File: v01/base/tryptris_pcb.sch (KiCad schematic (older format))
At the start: 131 parts, among them J1 USB_C_Receptacle_USB2.0, J2 I2C-L, J3 I2C-R, SW1 Reset, U1 ATmega32U4-AU, U2 MCP23017_SO, Y1 16Mhz

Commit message: Update base model to use parts from lcsc
The footprints for USB ports had to change as I can't get the previous
footprint shape from lcsc.
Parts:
- J1, J2, J3: footprint Type-C:USB_C_GCT_USB4085 -> Connector_USB:USB_C_Receptacle_HRO_TYPE-C-31-M-12
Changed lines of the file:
@@
 F 0 "J1" H 5207 2517 50  0000 C CNN
 F 1 "USB_C_Receptacle_USB2.0" H 5207 2426 50  0000 C CNN
-F 2 "Type-C:USB_C_GCT_USB4085" H 5250 1650 50  0001 C CNN
+F 2 "Connector_USB:USB_C_Receptacle_HRO_TYPE-C-31-M-12" H 5250 1650 50  0001 C CNN
 F 3 "https://www.usb.org/sites/default/files/documents/usb_type-c.zip" H 5250 1650 50  0001 C CNN
 	1    5100 1650
@@
 F 0 "J2" H 5357 5917 50  0000 C CNN
 F 1 "I2C-L" H 5357 5826 50  0000 C CNN
-F 2 "Type-C:USB_C_GCT_USB4085" H 5400 5050 50  0001 C CNN
+F 2 "Connector_USB:USB_C_Receptacle_HRO_TYPE-C-31-M-12" H 5400 5050 50  0001 C CNN
 F 3 "https://www.usb.org/sites/default/files/documents/usb_type-c.zip" H 5400 5050 50  0001 C CNN
 	1    5250 5050
@@
 F 0 "J3" H 4907 8217 50  0000 C CNN
 F 1 "I2C-R" H 4907 8126 50  0000 C CNN
-F 2 "Type-C:USB_C_GCT_USB4085" H 4950 7350 50  0001 C CNN
+F 2 "Connector_USB:USB_C_Receptacle_HRO_TYPE-C-31-M-12" H 4950 7350 50  0001 C CNN
 F 3 "https://www.usb.org/sites/default/files/documents/usb_type-c.zip" H 4950 7350 50  0001 C CNN
 	1    4800 7350

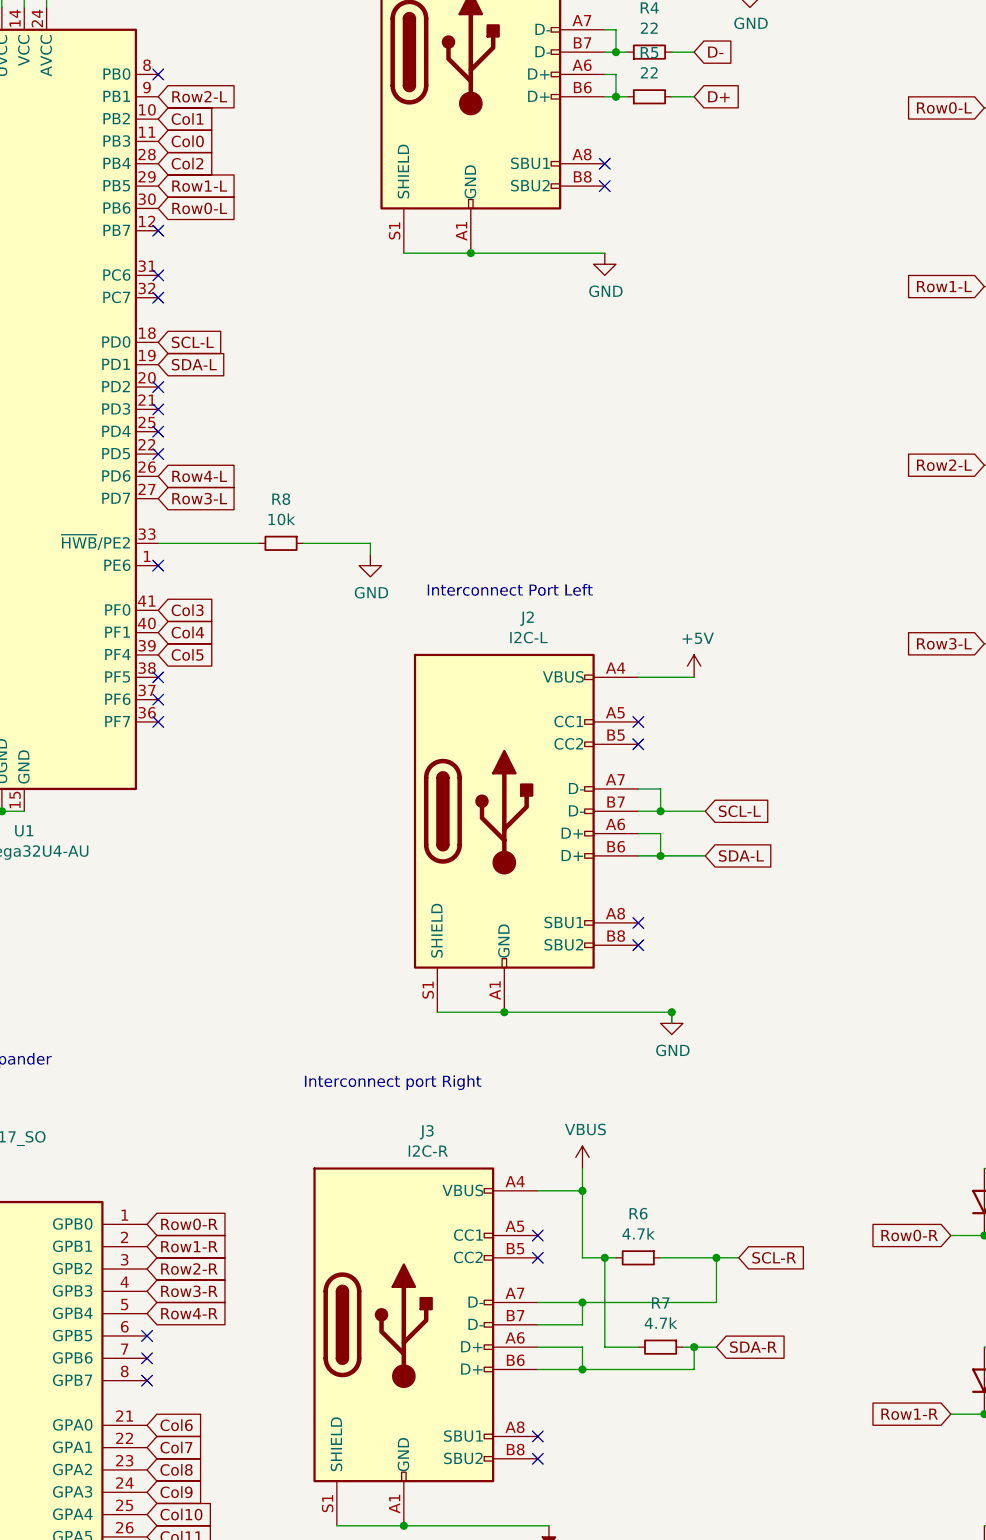
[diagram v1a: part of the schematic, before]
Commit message: Move I2C resistors to MCU side
This lets the right side be simpler and visually cleaner. It also
matches the component layout of the bling version.
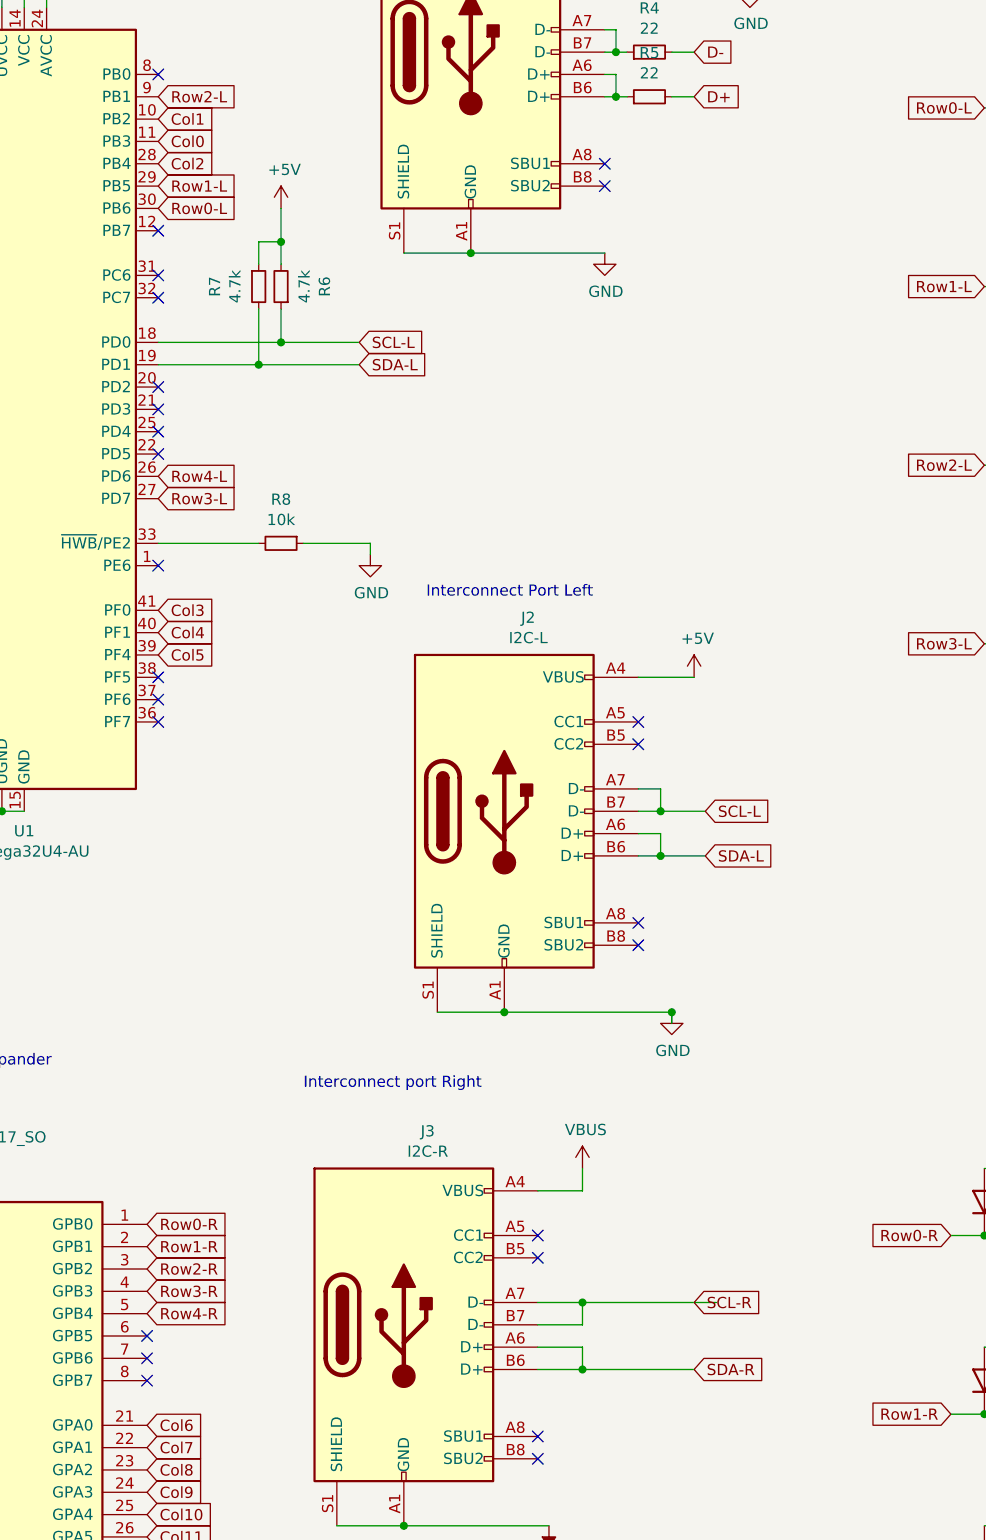
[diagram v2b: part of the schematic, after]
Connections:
- net +5V: now also R6.2, R7.1
- net SCL-L: now also R6.1
- net SCL-R: no longer R6.1
- net SDA-L: now also R7.2
- net SDA-R: no longer R7.1
- net VBUS: no longer R6.2, R7.2
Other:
- moved on the sheet: R6, R7
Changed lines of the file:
@@
 Text GLabel 2250 7000 0    50   Input ~ 0
 SCL-R
-Text GLabel 3700 3050 2    50   Input ~ 0
+Text GLabel 4600 3050 2    50   Input ~ 0
 SDA-L
-Text GLabel 3700 2950 2    50   Input ~ 0
+Text GLabel 4600 2950 2    50   Input ~ 0
 SCL-L
 Text Notes 4350 6300 0    50   ~ 0
@@
 Wire Wire Line
 	5600 6750 5600 6650
-Wire Wire Line
-	5600 7050 5700 7050
-Wire Wire Line
-	6200 7050 6300 7050
-Connection ~ 6200 7050
-Wire Wire Line
-	5950 7050 6200 7050
 $Comp
 L Device:R_Small R6
 U 1 1 615E83A9
-P 5850 7050
-F 0 "R6" V 5654 7050 50  0000 C CNN
-F 1 "4.7k" V 5745 7050 50  0000 C CNN
-F 2 "Resistor_SMD:R_0805_2012Metric" H 5850 7050 50  0001 C CNN
-F 3 "~" H 5850 7050 50  0001 C CNN
-	1    5850 7050
-	0    1    1    0
-$EndComp
-Text GLabel 6300 7050 2    50   Input ~ 0
+P 4250 2700
+F 0 "R6" V 4054 2700 50  0000 C CNN
+F 1 "4.7k" V 4145 2700 50  0000 C CNN
+F 2 "Resistor_SMD:R_0805_2012Metric" H 4250 2700 50  0001 C CNN
+F 3 "~" H 4250 2700 50  0001 C CNN
+	1    4250 2700
+	-1   0    0    1
+$EndComp
+Text GLabel 6100 7250 2    50   Input ~ 0
 SCL-R
 Wire Wire Line
 	5600 7250 6200 7250
-Wire Wire Line
-	6200 7050 6200 7250
 Connection ~ 5600 7250
-Wire Wire Line
-	5600 6750 5600 7050
-Connection ~ 5600 6750
-Wire Wire Line
-	6100 7450 6200 7450
-Connection ~ 6100 7450
-Wire Wire Line
-	6100 7550 6100 7450
-Wire Wire Line
-	6050 7450 6100 7450
 $Comp
 L Device:R_Small R7
 U 1 1 61698CA9
-P 5950 7450
-F 0 "R7" V 5754 7450 50  0000 C CNN
-F 1 "4.7k" V 5845 7450 50  0000 C CNN
-F 2 "Resistor_SMD:R_0805_2012Metric" H 5950 7450 50  0001 C CNN
-F 3 "~" H 5950 7450 50  0001 C CNN
-	1    5950 7450
-	0    1    1    0
-$EndComp
-Text GLabel 6200 7450 2    50   Input ~ 0
+P 4150 2700
+F 0 "R7" V 3954 2700 50  0000 C CNN
+F 1 "4.7k" V 4045 2700 50  0000 C CNN
+F 2 "Resistor_SMD:R_0805_2012Metric" H 4150 2700 50  0001 C CNN
+F 3 "~" H 4150 2700 50  0001 C CNN
+	1    4150 2700
+	1    0    0    -1
+$EndComp
+Text GLabel 6100 7550 2    50   Input ~ 0
 SDA-R
 Wire Wire Line
 	5600 7550 6100 7550
 Connection ~ 5600 7550
-Wire Wire Line
-	5700 7050 5700 7450
-Wire Wire Line
-	5700 7450 5850 7450
-Connection ~ 5700 7050
-Wire Wire Line
-	5700 7050 5750 7050
 NoConn ~ 5850 5550
 NoConn ~ 5850 5650
@@
 NoConn ~ 5400 7850
 NoConn ~ 5400 7950
+Wire Wire Line
+	3700 2950 4250 2950
+Wire Wire Line
+	3700 3050 4150 3050
+Wire Wire Line
+	4150 2800 4150 3050
+Connection ~ 4150 3050
+Wire Wire Line
+	4150 3050 4600 3050
+Wire Wire Line
+	4250 2800 4250 2950
+Connection ~ 4250 2950
+Wire Wire Line
+	4250 2950 4600 2950
+$Comp
+L power:+5V #PWR?
+U 1 1 617063DF
+P 4250 2350
+F 0 "#PWR?" H 4250 2200 50  0001 C CNN
+F 1 "+5V" H 4265 2523 50  0000 C CNN
+F 2 "" H 4250 2350 50  0001 C CNN
+F 3 "" H 4250 2350 50  0001 C CNN
+	1    4250 2350
+	1    0    0    -1
+$EndComp
+Wire Wire Line
+	4250 2350 4250 2500
+Wire Wire Line
+	4250 2500 4150 2500
+Wire Wire Line
+	4150 2500 4150 2600
+Connection ~ 4250 2500
+Wire Wire Line
+	4250 2500 4250 2600
 $EndSCHEMATC

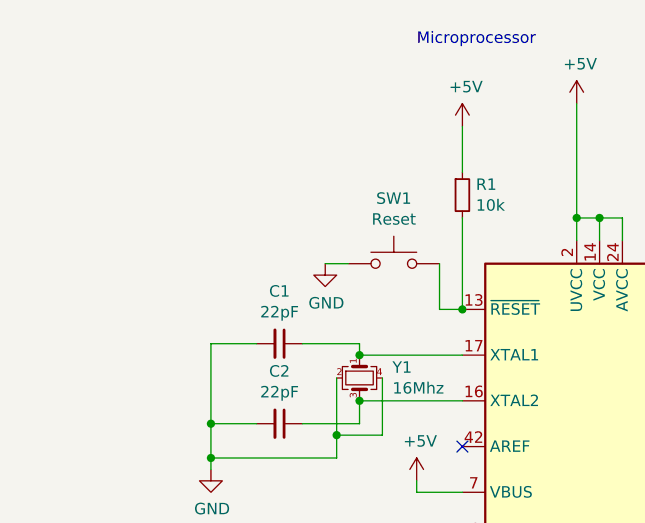
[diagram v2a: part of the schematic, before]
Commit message: Add ISP connector to base board.
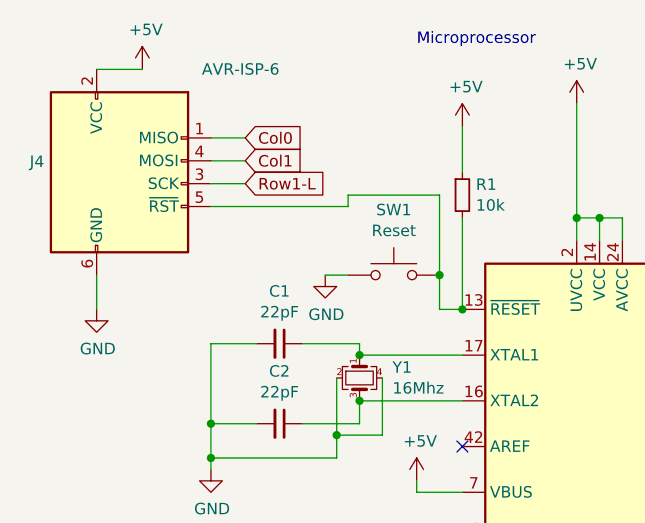
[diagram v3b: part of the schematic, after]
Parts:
- added J4: AVR-ISP-6, random-keyboard-parts:Reset_Pretty-Mask, symbol Connector:AVR-ISP-6
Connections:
- net +5V: now also J4.2 (VCC)
- net Col0: now also J4.1 (MISO)
- net Col1: now also J4.4 (MOSI)
- net GND: now also J4.6 (GND)
- net Row1-L: now also J4.3 (SCK)
- net at R1.2, SW1.2, U1.13 (~RESET): now also J4.5 (~RST)
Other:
- moved on the sheet: SW1
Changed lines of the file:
@@
 $EndDescr
-$Comp
-L MCU_Microchip_ATmega:ATmega32U4-AU U1
-U 1 1 60F2601E
-P 3100 3250
-F 0 "U1" H 3100 1361 50  0000 C CNN
-F 1 "ATmega32U4-AU" H 3100 1270 50  0000 C CNN
-F 2 "Package_QFP:TQFP-44_10x10mm_P0.8mm" H 3100 3250 50  0001 C CIN
-F 3 "http://ww1.microchip.com/downloads/en/DeviceDoc/Atmel-7766-8-bit-AVR-ATmega16U4-32U4_Datasheet.pdf" H 3100 3250 50  0001 C CNN
-	1    3100 3250
-	1    0    0    -1
-$EndComp
 $Comp
 L power:+5V #PWR0101
@@
 L Switch:SW_Push SW1
 U 1 1 60F454A1
-P 2200 1550
-F 0 "SW1" H 2200 1835 50  0000 C CNN
-F 1 "Reset" H 2200 1744 50  0000 C CNN
-F 2 "Keebio-Parts:SW_SPST_TL3342" H 2200 1750 50  0001 C CNN
-F 3 "~" H 2200 1750 50  0001 C CNN
-	1    2200 1550
-	1    0    0    -1
-$EndComp
-Wire Wire Line
-	2400 1550 2400 1750
-Wire Wire Line
-	2400 1750 2500 1750
+P 2200 1600
+F 0 "SW1" H 2200 1885 50  0000 C CNN
+F 1 "Reset" H 2200 1794 50  0000 C CNN
+F 2 "Keebio-Parts:SW_SPST_TL3342" H 2200 1800 50  0001 C CNN
+F 3 "~" H 2200 1800 50  0001 C CNN
+	1    2200 1600
+	1    0    0    -1
+$EndComp
 $Comp
 L power:GND #PWR0109
 U 1 1 60F49E63
-P 1900 1550
-F 0 "#PWR0109" H 1900 1300 50  0001 C CNN
-F 1 "GND" H 1905 1377 50  0000 C CNN
-F 2 "" H 1900 1550 50  0001 C CNN
-F 3 "" H 1900 1550 50  0001 C CNN
-	1    1900 1550
-	1    0    0    -1
-$EndComp
-Wire Wire Line
-	1900 1550 2000 1550
+P 1900 1600
+F 0 "#PWR0109" H 1900 1350 50  0001 C CNN
+F 1 "GND" H 1905 1427 50  0000 C CNN
+F 2 "" H 1900 1600 50  0001 C CNN
+F 3 "" H 1900 1600 50  0001 C CNN
+	1    1900 1600
+	1    0    0    -1
+$EndComp
+Wire Wire Line
+	1900 1600 2000 1600
 $Comp
 L Device:R_Small R1
@@
 Wire Wire Line
 	2500 1750 2500 1350
-Connection ~ 2500 1750
 $Comp
 L power:+5V #PWR0110
@@
 	4250 2950 4600 2950
 $Comp
-L power:+5V #PWR?
+L power:+5V #PWR0127
 U 1 1 617063DF
 P 4250 2350
-F 0 "#PWR?" H 4250 2200 50  0001 C CNN
+F 0 "#PWR0127" H 4250 2200 50  0001 C CNN
 F 1 "+5V" H 4265 2523 50  0000 C CNN
 F 2 "" H 4250 2350 50  0001 C CNN
@@
 Wire Wire Line
 	4250 2500 4250 2600
+$Comp
+L Connector:AVR-ISP-6 J4
+U 1 1 617A0942
+P 1000 1200
+F 0 "J4" H 671 1296 50  0000 R CNN
+F 1 "AVR-ISP-6" H 1700 1700 50  0000 R CNN
+F 2 "random-keyboard-parts:Reset_Pretty-Mask" V 750 1250 50  0001 C CNN
+F 3 " ~" H -275 650 50  0001 C CNN
+	1    1000 1200
+	1    0    0    -1
+$EndComp
+$Comp
+L power:GND #PWR0128
+U 1 1 617A5F51
+P 900 1750
+F 0 "#PWR0128" H 900 1500 50  0001 C CNN
+F 1 "GND" H 905 1577 50  0000 C CNN
+F 2 "" H 900 1750 50  0001 C CNN
+F 3 "" H 900 1750 50  0001 C CNN
+	1    900  1750
+	1    0    0    -1
+$EndComp
+Wire Wire Line
+	900  1750 900  1600
+$Comp
+L power:+5V #PWR0129
+U 1 1 617BE7E7
+P 1100 700
+F 0 "#PWR0129" H 1100 550 50  0001 C CNN
+F 1 "+5V" H 1115 873 50  0000 C CNN
+F 2 "" H 1100 700 50  0001 C CNN
+F 3 "" H 1100 700 50  0001 C CNN
+	1    1100 700
+	1    0    0    -1
+$EndComp
+Wire Wire Line
+	1100 700  900  700
+Text GLabel 1550 1100 2    50   Input ~ 0
+Col1
+Wire Wire Line
+	1550 1100 1400 1100
+Text GLabel 1550 1000 2    50   Input ~ 0
+Col0
+Wire Wire Line
+	1550 1000 1400 1000
+Text GLabel 1550 1200 2    50   Input ~ 0
+Row1-L
+Wire Wire Line
+	1400 1200 1550 1200
+$Comp
+L MCU_Microchip_ATmega:ATmega32U4-AU U1
+U 1 1 60F2601E
+P 3100 3250
+F 0 "U1" H 3100 1361 50  0000 C CNN
+F 1 "ATmega32U4-AU" H 3100 1270 50  0000 C CNN
+F 2 "Package_QFP:TQFP-44_10x10mm_P0.8mm" H 3100 3250 50  0001 C CIN
+F 3 "http://ww1.microchip.com/downloads/en/DeviceDoc/Atmel-7766-8-bit-AVR-ATmega16U4-32U4_Datasheet.pdf" H 3100 3250 50  0001 C CNN
+	1    3100 3250
+	1    0    0    -1
+$EndComp
+Wire Wire Line
+	2500 1750 2400 1750
+Wire Wire Line
+	2400 1750 2400 1600
+Connection ~ 2500 1750
+Wire Wire Line
+	2400 1600 2400 1250
+Wire Wire Line
+	2400 1250 2000 1250
+Wire Wire Line
+	2000 1250 2000 1300
+Wire Wire Line
+	2000 1300 1400 1300
+Connection ~ 2400 1600
 $EndSCHEMATC

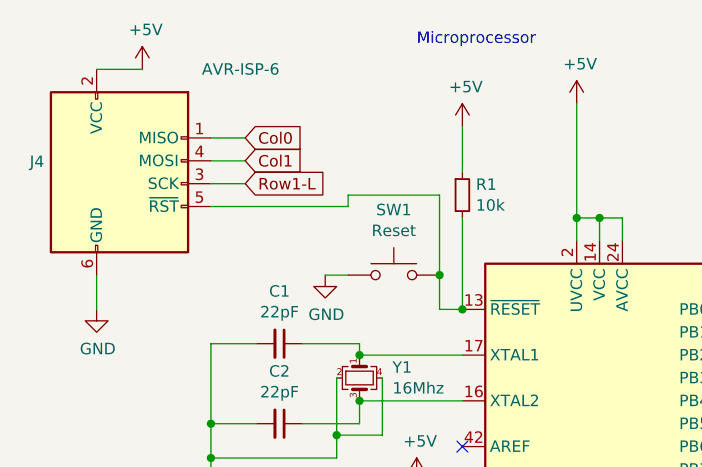
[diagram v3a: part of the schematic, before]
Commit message: Fix ISP wiring
I got the pins wrong.
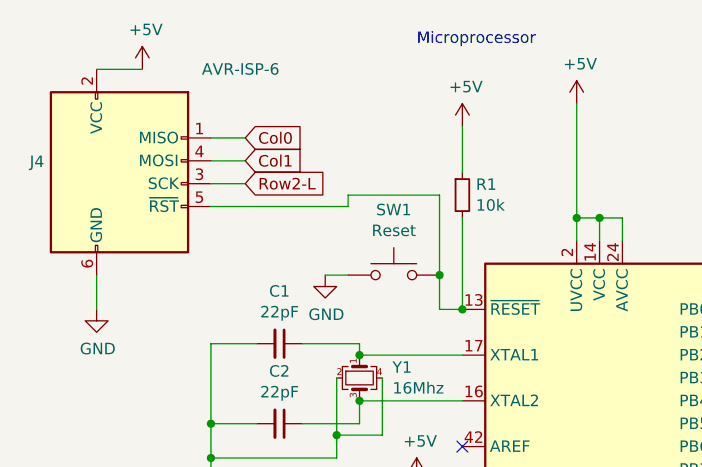
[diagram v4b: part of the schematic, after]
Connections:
- net Row1-L: no longer J4.3 (SCK)
- net Row2-L: now also J4.3 (SCK)
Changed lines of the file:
@@
 	1550 1000 1400 1000
 Text GLabel 1550 1200 2    50   Input ~ 0
-Row1-L
+Row2-L
 Wire Wire Line
 	1400 1200 1550 1200
